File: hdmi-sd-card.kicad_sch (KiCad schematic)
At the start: 92 parts, among them J11 I-PEX_CABLINE-VS_1x20_20455-A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, J4 HDMI-A_WE_685119134923, J5 MicroSD_693071020811, Q18 BSS138PW, Q19 BSS138PW, Q21 BSS138PW, U10 TPD4E05U06QDQARQ1, U11 TPD4E05U06QDQARQ1, U12 TPD4E05U06QDQARQ1, U14 TPD4E05U06QDQARQ1, U37 TPD4E05U06QDQARQ1, U38 SN65DP159RGZR, U40 NVT4858_XQFN, U41 TPD4E05U06QDQARQ1, U42 M24C64-F_DFN8, U43 TPS2116DRLR, U44 TXS0102DQER, U47 TPD4E05U06QDQARQ1, U48 TPD4E05U06QDQARQ1

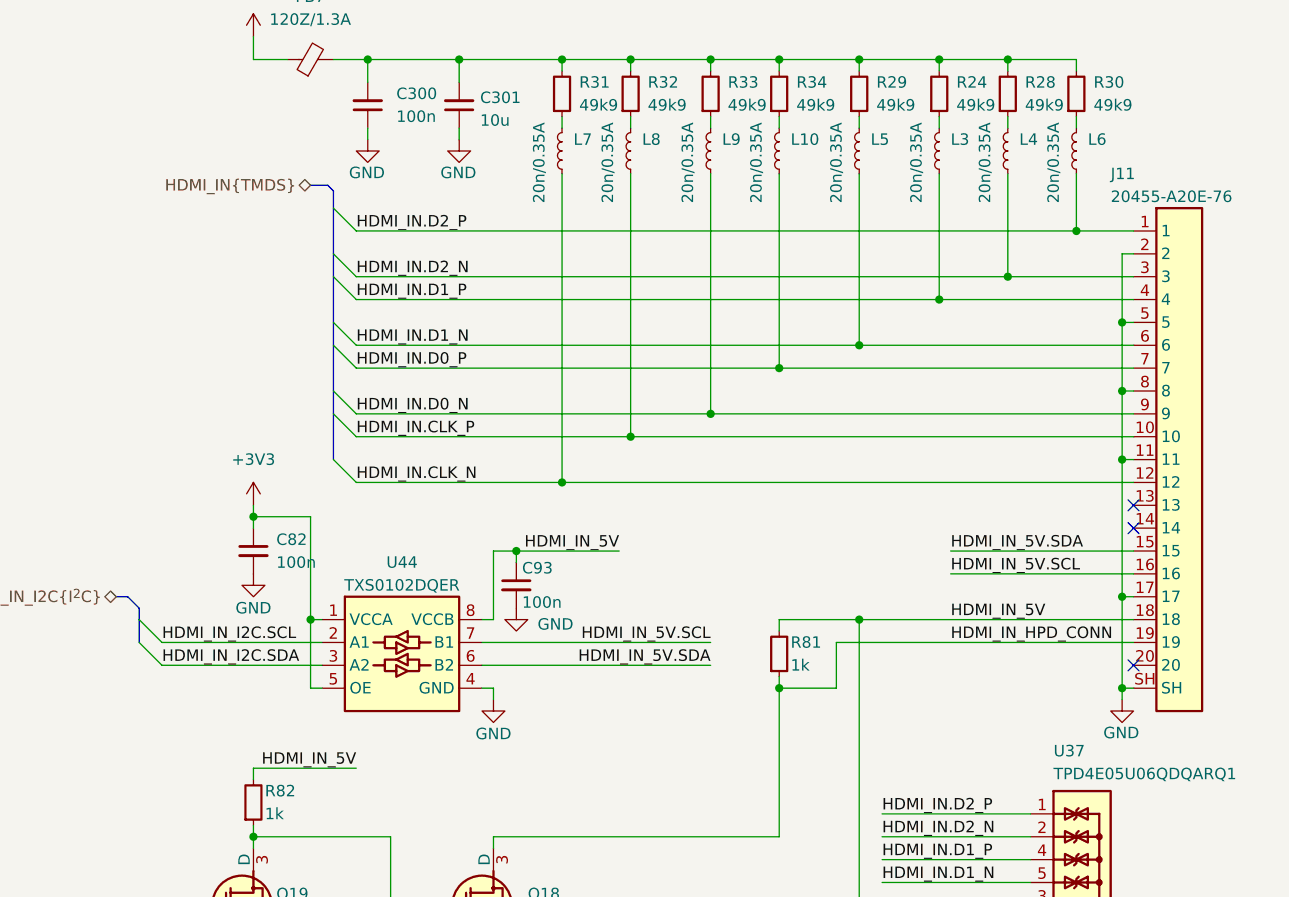
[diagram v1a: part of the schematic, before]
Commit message: [#65754] Route HDMI
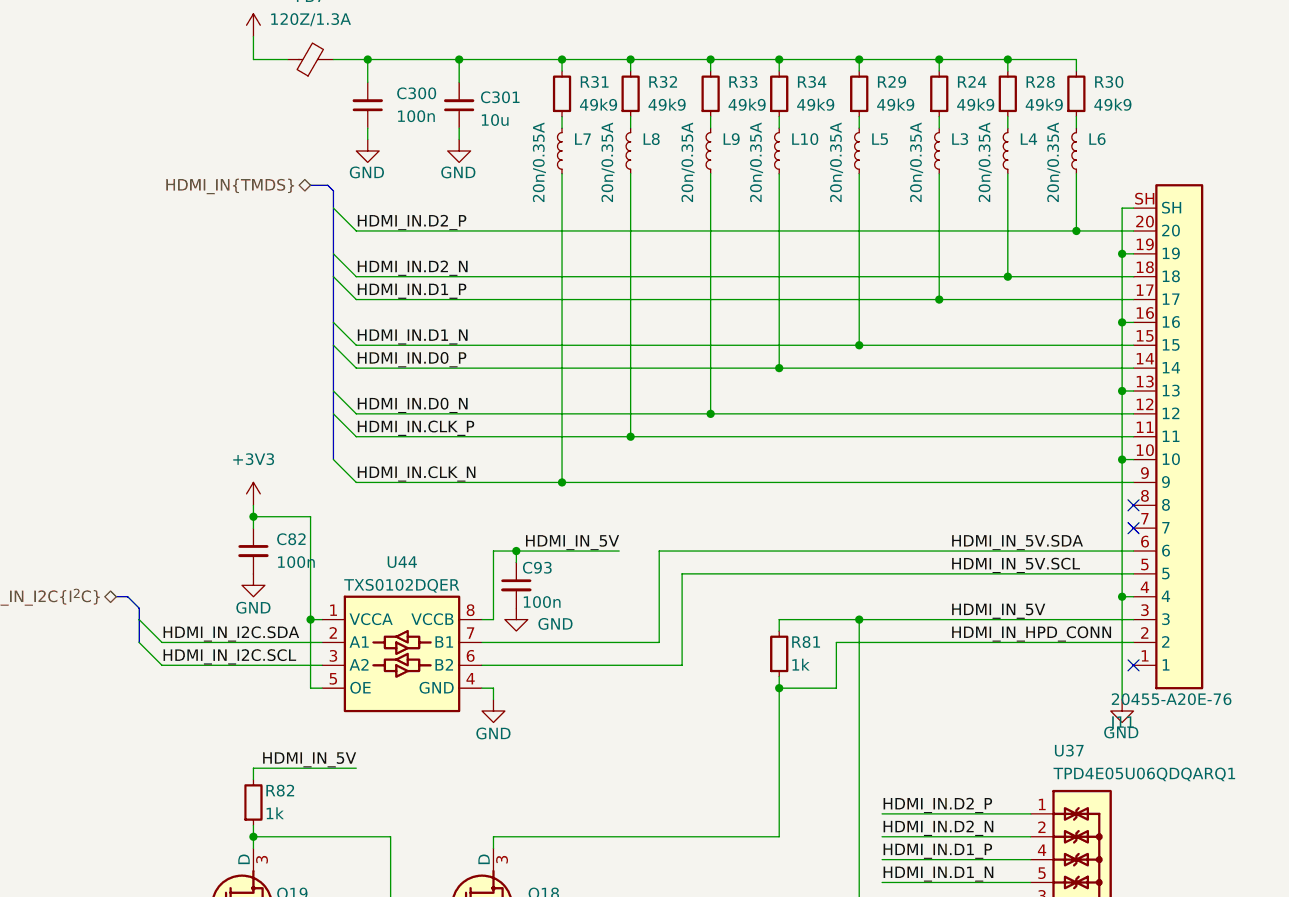
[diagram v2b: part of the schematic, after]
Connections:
- net GND: now also J11.10, J11.13, J11.16, J11.19, J11.4; no longer J11.11, J11.17, J11.2, J11.5, J11.8
- net HDMI_IN.CLK_N: now also J11.9; no longer J11.12
- net HDMI_IN.CLK_P: now also J11.11; no longer J11.10
- net HDMI_IN.D0_N: now also J11.12; no longer J11.9
- net HDMI_IN.D0_P: now also J11.14; no longer J11.7
- net HDMI_IN.D1_N: now also J11.15; no longer J11.6
- net HDMI_IN.D1_P: now also J11.17; no longer J11.4
- net HDMI_IN.D2_N: now also J11.18; no longer J11.3
- net HDMI_IN.D2_P: now also J11.20; no longer J11.1
- net HDMI_IN_5V: now also J11.3; no longer J11.18
- net HDMI_IN_5V.SCL: now also J11.5, U44.6 (B2); no longer J11.16, U44.7 (B1)
- net HDMI_IN_5V.SDA: now also J11.6, U44.7 (B1); no longer J11.15, U44.6 (B2)
- net HDMI_IN_HPD_CONN: now also J11.2; no longer J11.19
- net HDMI_IN_I2C.SCL: now also U44.3 (A2); no longer U44.2 (A1)
- net HDMI_IN_I2C.SDA: now also U44.2 (A1); no longer U44.3 (A2)
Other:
- moved on the sheet: J11
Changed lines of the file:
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@@
   (junction (at 212.725 243.84) (diameter 0) (color 0 0 0 0)
   )
+  (junction (at 391.16 49.53) (diameter 0) (color 0 0 0 0)
+  )
   (junction (at 378.46 27.94) (diameter 0) (color 0 0 0 0)
   )
@@
   (junction (at 261.62 248.92) (diameter 0) (color 0 0 0 0)
   )
-  (junction (at 391.16 97.79) (diameter 0) (color 0 0 0 0)
-  )
   (junction (at 132.08 275.59) (diameter 0) (color 0 0 0 0)
   )
@@
     (stroke (width 0) (type default))
   )
+  (wire (pts (xy 391.16 44.45) (xy 392.43 44.45))
+    (stroke (width 0) (type default))
+  )
   (wire (pts (xy 353.06 90.17) (xy 361.95 90.17))
     (stroke (width 0) (type default))
@@
     (stroke (width 0) (type default))
   )
-  (wire (pts (xy 391.16 97.79) (xy 392.43 97.79))
-    (stroke (width 0) (type default))
-  )
   (wire (pts (xy 97.79 275.59) (xy 92.71 275.59))
     (stroke (width 0) (type default))
@@
     (stroke (width 0) (type default))
   )
-  (wire (pts (xy 320.04 95.25) (xy 345.44 95.25))
+  (wire (pts (xy 320.04 95.25) (xy 342.265 95.25))
     (stroke (width 0) (type default))
   )
@@
     (stroke (width 0) (type default))
   )
-  (wire (pts (xy 372.11 85.09) (xy 392.43 85.09))
+  (wire (pts (xy 342.265 85.09) (xy 392.43 85.09))
     (stroke (width 0) (type default))
   )
@@
     (stroke (width 0) (type default))
   )
-  (wire (pts (xy 372.11 82.55) (xy 392.43 82.55))
+  (wire (pts (xy 339.725 82.55) (xy 392.43 82.55))
     (stroke (width 0) (type default))
   )
@@
     (stroke (width 0) (type default))
   )
+  (wire (pts (xy 342.265 85.09) (xy 342.265 95.25))
+    (stroke (width 0) (type default))
+  )
   (wire (pts (xy 76.2 153.67) (xy 76.2 156.21))
     (stroke (width 0) (type default))
@@
     (stroke (width 0) (type default))
   )
-  (wire (pts (xy 391.16 87.63) (xy 391.16 97.79))
-    (stroke (width 0) (type default))
-  )
   (wire (pts (xy 256.54 238.76) (xy 256.54 241.3))
     (stroke (width 0) (type default))
@@
     (stroke (width 0) (type default))
   )
+  (wire (pts (xy 391.16 49.53) (xy 391.16 44.45))
+    (stroke (width 0) (type default))
+  )
   (wire (pts (xy 336.55 69.85) (xy 392.43 69.85))
     (stroke (width 0) (type default))
@@
     (stroke (width 0) (type default))
   )
+  (wire (pts (xy 339.725 82.55) (xy 339.725 92.71))
+    (stroke (width 0) (type default))
+  )
   (wire (pts (xy 207.01 218.44) (xy 229.87 218.44))
     (stroke (width 0) (type default))
@@
     (stroke (width 0) (type default))
   )
-  (wire (pts (xy 320.04 92.71) (xy 345.44 92.71))
+  (wire (pts (xy 320.04 92.71) (xy 339.725 92.71))
     (stroke (width 0) (type default))
   )
@@
     (stroke (width 0) (type default))
   )
-  (wire (pts (xy 391.16 97.79) (xy 391.16 99.06))
+  (wire (pts (xy 391.16 87.63) (xy 391.16 99.06))
     (stroke (width 0) (type default))
   )
@@
     (effects (font (size 2.9972 2.9972) (thickness 0.5994) bold) (justify left bottom))
   )
-  (label "HDMI_IN_5V.SCL" (at 345.44 92.71 180) (fields_autoplaced)
-    (effects (font (size 1.27 1.27)) (justify right bottom))
-  )
   (label "HDMI_OUT_CONN_D1_P" (at 207.01 200.66 0) (fields_autoplaced)
     (effects (font (size 1.27 1.27)) (justify left bottom))
@@
     (effects (font (size 1.27 1.27)) (justify left bottom))
   )
-  (label "HDMI_IN_5V.SDA" (at 345.44 95.25 180) (fields_autoplaced)
-    (effects (font (size 1.27 1.27)) (justify right bottom))
-  )
   (label "HDMI_IN_5V" (at 372.11 90.17 0) (fields_autoplaced)
     (effects (font (size 1.27 1.27)) (justify left bottom))
@@
     (effects (font (size 1.27 1.27)) (justify left bottom))
   )
-  (label "HDMI_IN_I2C.SCL" (at 284.48 92.71 0) (fields_autoplaced)
+  (label "HDMI_IN_I2C.SCL" (at 284.48 95.25 0) (fields_autoplaced)
     (effects (font (size 1.27 1.27)) (justify left bottom))
   )
@@
     (effects (font (size 1.27 1.27)) (justify left bottom))
   )
-  (label "HDMI_IN_I2C.SDA" (at 284.48 95.25 0) (fields_autoplaced)
+  (label "HDMI_IN_I2C.SDA" (at 284.48 92.71 0) (fields_autoplaced)
     (effects (font (size 1.27 1.27)) (justify left bottom))
   )
@@
     )
   )
-  (symbol (lib_id "antmicroWire2BoardConnectors:I-PEX_CABLINE-VS_1x20_20455-A20E-76") (at 392.43 46.99 0) (unit 1)
+  (symbol (lib_id "antmicroWire2BoardConnectors:I-PEX_CABLINE-VS_1x20_20455-A20E-76") (at 392.43 95.25 0) (mirror x) (unit 1)
     (in_bom yes) (on_board yes) (dnp no)
-    (property "Reference" "J11" (at 389.89 40.64 0)
+    (property "Reference" "J11" (at 389.89 101.6 0)
       (effects (font (size 1.27 1.27) (thickness 0.15)) (justify left))
     )
-    (property "Value" "I-PEX_CABLINE-VS_1x20_20455-A20E-76" (at 415.29 54.61 0)
+    (property "Value" "I-PEX_CABLINE-VS_1x20_20455-A20E-76" (at 415.29 87.63 0)
       (effects (font (size 1.27 1.27) (thickness 0.15)) (justify left bottom) hide)
     )
-    (property "Footprint" "antmicro-footprints:I-PEX_CABLINE-VS_1x20_20455-A20E-76" (at 415.29 57.15 0)
+    (property "Footprint" "antmicro-footprints:I-PEX_CABLINE-VS_1x20_20455-A20E-76" (at 415.29 85.09 0)
       (effects (font (size 1.27 1.27) (thickness 0.15)) (justify left bottom) hide)
     )
-    (property "Datasheet" "https://www.i-pex.com/sites/default/files/downloads/pdf/MANUAL_CABLINE-VS_HIM-08004-07EN.pdf" (at 415.29 59.69 0)
+    (property "Datasheet" "https://www.i-pex.com/sites/default/files/downloads/pdf/MANUAL_CABLINE-VS_HIM-08004-07EN.pdf" (at 415.29 82.55 0)
       (effects (font (size 1.27 1.27) (thickness 0.15)) (justify left bottom) hide)
     )
-    (property "MPN" "20455-A20E-76" (at 389.89 43.18 0)
+    (property "MPN" "20455-A20E-76" (at 389.89 99.06 0)
       (effects (font (size 1.27 1.27) (thickness 0.15)) (justify left))
     )
-    (property "Manufacturer" "I-PEX" (at 415.29 62.23 0)
+    (property "Manufacturer" "I-PEX" (at 415.29 80.01 0)
       (effects (font (size 1.27 1.27) (thickness 0.15)) (justify left bottom) hide)
     )
-    (property "Author" "Antmicro" (at 415.29 64.77 0)
+    (property "Author" "Antmicro" (at 415.29 77.47 0)
       (effects (font (size 1.27 1.27) (thickness 0.15)) (justify left bottom) hide)
     )
-    (property "License" "Apache-2.0" (at 415.29 67.31 0)
+    (property "License" "Apache-2.0" (at 415.29 74.93 0)
       (effects (font (size 1.27 1.27) (thickness 0.15)) (justify left bottom) hide)
     )

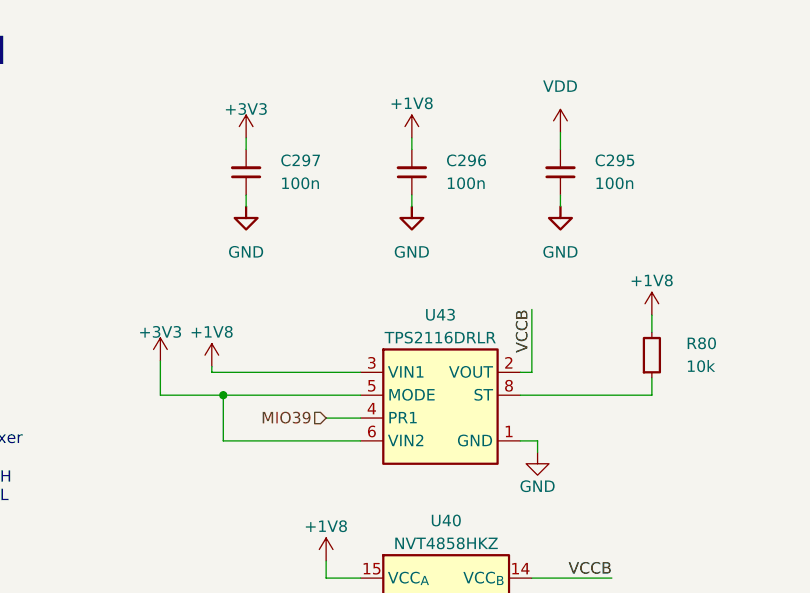
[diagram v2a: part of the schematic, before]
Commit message: [#66727] Minor schematic improvements. Finish routing right side of the board
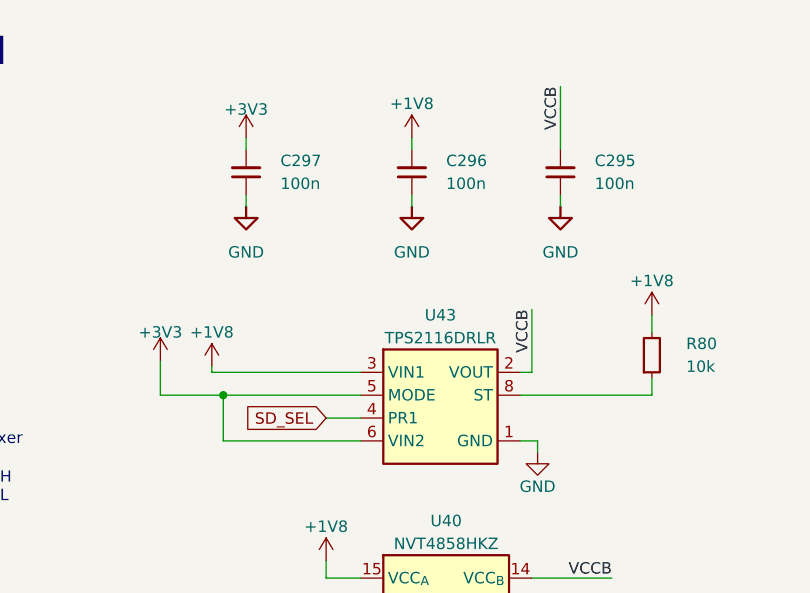
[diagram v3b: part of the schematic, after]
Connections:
- net +1V1: no longer C295.2
- net VCCB: now also C295.2
- net MIO39 renamed SD_SEL
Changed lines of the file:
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@@
     (stroke (width 0) (type default))
   )
-  (wire (pts (xy 102.235 27.305) (xy 102.235 25.4))
+  (wire (pts (xy 102.235 27.305) (xy 102.235 20.32))
     (stroke (width 0) (type default))
   )
@@
     (effects (font (size 1.27 1.27)) (justify left bottom))
   )
+  (label "VCCB" (at 102.235 20.32 270) (fields_autoplaced)
+    (effects (font (size 1.27 1.27)) (justify right bottom))
+  )
   (label "SD_CLK" (at 107.95 82.55 180) (fields_autoplaced)
     (effects (font (size 1.27 1.27)) (justify right bottom))
@@
     (effects (font (size 1.27 1.27)) (justify left bottom))
   )
+  (global_label "SD_SEL" (shape input) (at 76.2 57.15 180) (fields_autoplaced)
+    (effects (font (size 1.27 1.27)) (justify right))
+    (property "Intersheetrefs" "${INTERSHEET_REFS}" (at 66.3811 57.15 0)
+      (effects (font (size 1.27 1.27)) (justify right))
+    )
+  )
   (global_label "HDMI_OE" (shape input) (at 52.07 224.79 180) (fields_autoplaced)
     (effects (font (size 1.27 1.27)) (justify right))
@@
     (effects (font (size 1.27 1.27)) (justify right))
   )
-  (hierarchical_label "MIO39" (shape input) (at 76.2 57.15 180) (fields_autoplaced)
-    (effects (font (size 1.27 1.27)) (justify right))
-  )
   (hierarchical_label "SD{SDIO}" (shape bidirectional) (at 26.67 75.565 180) (fields_autoplaced)
     (effects (font (size 1.27 1.27)) (justify right))
@@
         )
       )
-    )
-  )
-  (symbol (lib_id "antmicropower:VDD") (at 102.235 25.4 0) (unit 1)
-    (in_bom yes) (on_board yes) (dnp no) (fields_autoplaced)
-    (property "Reference" "#PWR0491" (at 102.235 29.21 0)
-      (effects (font (size 1.27 1.27)) hide)
-    )
-    (property "Value" "VDD" (at 102.235 20.32 0)
-      (effects (font (size 1.27 1.27)))
-    )
-    (property "Footprint" "" (at 102.235 25.4 0)
-      (effects (font (size 1.27 1.27)) hide)
-    )
-    (property "Datasheet" "" (at 102.235 25.4 0)
-      (effects (font (size 1.27 1.27)) hide)
-    )
-    (pin "1")
-    (instances
-      (project "data-center-rdimm-ddr5-tester"
-        (path "/1faa6543-e26a-4449-8bac-ee14b9f19e5f/59a8849d-b77a-4f79-b7ae-cd57b3cb4d28"
-          (reference "#PWR0491") (unit 1)
-        )
-      )

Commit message: [#67725] Update HDMI and SDcard
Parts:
- removed U12, U14: TPD4E05U06QDQARQ1, antmicro-footprints:USON-10_2.5x1mm_P0.5mm, symbol antmicroTVSDiodes:TPD4E05U06QDQARQ1
- added D19: PESD5V0X1UB, antmicro-footprints:SOD-523, symbol antmicroTVSDiodes:PESD5V0X1UB
- added R234, R236, R237, R239: R_2k2_0402, antmicro-footprints:R_0402_1005Metric, symbol antmicroResistors0402:R_2k2_0402
- R225: now not fitted
- R77: now fitted
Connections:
- net +3V3: now also R234.2, R236.2, R237.2, R239.2
- net GND: now also D19.2 (A)
- net HDMI_CTL.SCL: now also R239.1
- net HDMI_CTL.SDA: now also R234.1
- net HDMI_OUT_I2C.SCL: now also R236.1
- net HDMI_OUT_I2C.SDA: now also R237.1
- net SD.CD: now also D19.1 (C)
- no-connect marks 10 -> 9
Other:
- note added: "Decoupling"
- note added: "EEPROM"
- note added: "HDMI input connector"
- note added: "HDMI output connector"
- note added: "HDMI retimer"
- note added: "Logic level translator"
- note added: "TVS IN"
- note added: "TVS OUT"
- note added: "Voltage level translator"
- note added: "uSD card slot"
- moved on the sheet: C126, C129, C132, C273, C274, C277, C278, C280, C281, C282, C283, C284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

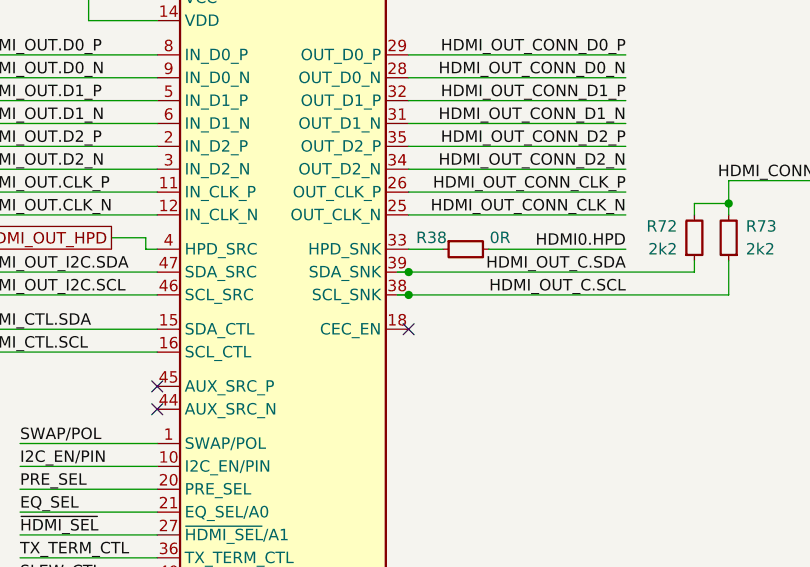
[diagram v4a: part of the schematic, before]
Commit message: [#67725] Import review changes to PCB. Minor schematic fix
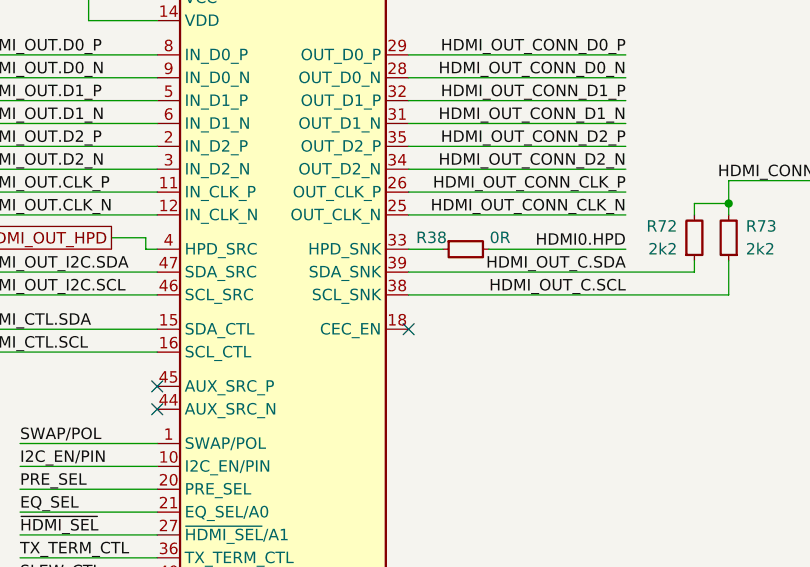
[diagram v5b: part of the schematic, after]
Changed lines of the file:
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@@
   (junction (at 78.74 274.32) (diameter 0) (color 0 0 0 0)
   )
-  (junction (at 109.22 186.69) (diameter 0) (color 0 0 0 0)
-  )
   (junction (at 57.15 224.79) (diameter 0) (color 0 0 0 0)
   )
@@
   )
   (junction (at 353.06 31.75) (diameter 0) (color 0 0 0 0)
-  )
-  (junction (at 109.22 189.23) (diameter 0) (color 0 0 0 0)
   )
   (junction (at 78.74 276.86) (diameter 0) (color 0 0 0 0)
@@
     (stroke (width 0) (type default))
   )
-  (wire (pts (xy 107.95 186.69) (xy 109.22 186.69))
-    (stroke (width 0) (type default))
-  )
   (wire (pts (xy 328.93 38.1) (xy 328.93 40.64))
     (stroke (width 0) (type default))
@@
     (stroke (width 0) (type default))
   )
-  (wire (pts (xy 107.95 189.23) (xy 109.22 189.23))
-    (stroke (width 0) (type default))
-  )
